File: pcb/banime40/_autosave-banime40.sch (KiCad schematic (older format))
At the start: 85 parts, among them SW1 SW_SPST, SW10 SW_SPST, SW11 SW_SPST, SW12 SW_SPST, SW13 SW_SPST, SW14 SW_SPST, SW15 SW_SPST, SW16 SW_SPST, SW17 SW_SPST, SW18 SW_SPST, SW19 SW_SPST, SW2 SW_SPST, SW20 SW_SPST, SW21 SW_SPST, SW22 SW_SPST, SW23 SW_SPST, SW24 SW_SPST, SW25 SW_SPST, SW26 SW_SPST, SW27 SW_SPST, SW28 SW_SPST, SW29 SW_SPST, SW3 SW_SPST, SW30 SW_SPST, SW31 SW_SPST, SW32 SW_SPST, SW33 SW_SPST, SW34 SW_SPST, SW35 SW_SPST, SW36 SW_SPST, SW37 SW_SPST, SW38 SW_SPST, SW39 SW_SPST, SW4 SW_SPST, SW40 SW_SPST, SW41 SW_SPST, SW42 SW_SPST, SW43 SW_SPST, SW44 SW_SPST, SW5 SW_SPST, SW6 SW_SPST, SW7 SW_SPST, SW8 SW_SPST, SW9 SW_SPST, U1 ProMicro

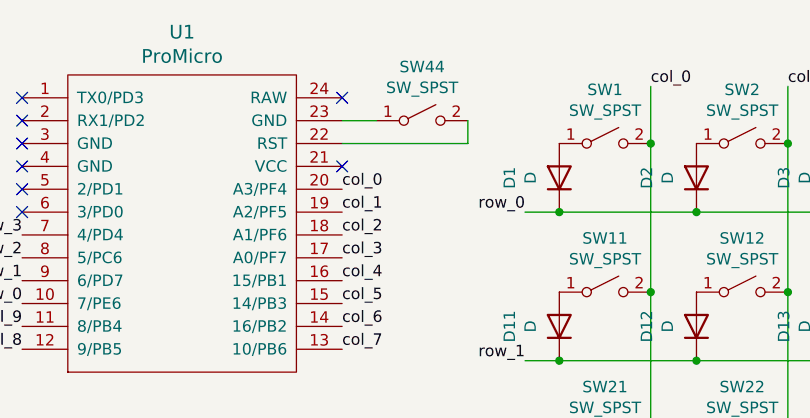
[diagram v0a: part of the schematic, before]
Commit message: update board, add spacebar layout
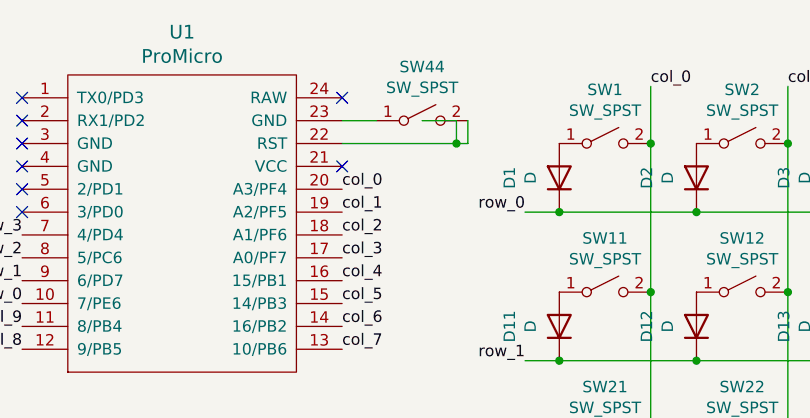
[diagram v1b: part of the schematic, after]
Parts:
- SW44: footprint Keebio:SW_SPST_TL3342 -> Keebio:SW_SPST_3x3
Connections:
- wire segments 103 -> 106
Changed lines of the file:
@@
 F 0 "SW44" H 2750 1435 50  0000 C CNN
 F 1 "SW_SPST" H 2750 1344 50  0000 C CNN
-F 2 "Keebio:SW_SPST_TL3342" H 2750 1200 50  0001 C CNN
+F 2 "Keebio:SW_SPST_3x3" H 2750 1200 50  0001 C CNN
 F 3 "~" H 2750 1200 50  0001 C CNN
 	1    2750 1200
@@
 	2400 1200 2550 1200
 Wire Wire Line
-	2400 1300 2950 1300
+	2400 1300 2900 1300
 Wire Wire Line
 	2950 1300 2950 1200
+Wire Wire Line
+	2900 1300 2900 1200
+Wire Wire Line
+	2900 1200 2750 1200
+Connection ~ 2900 1300
+Wire Wire Line
+	2900 1300 2950 1300
 $EndSCHEMATC
